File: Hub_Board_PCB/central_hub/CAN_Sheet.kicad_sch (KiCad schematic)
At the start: 18 parts, among them J1 CAN_OUT, U3 MCP2515-xST, U4 TJA1050, Y2 8M

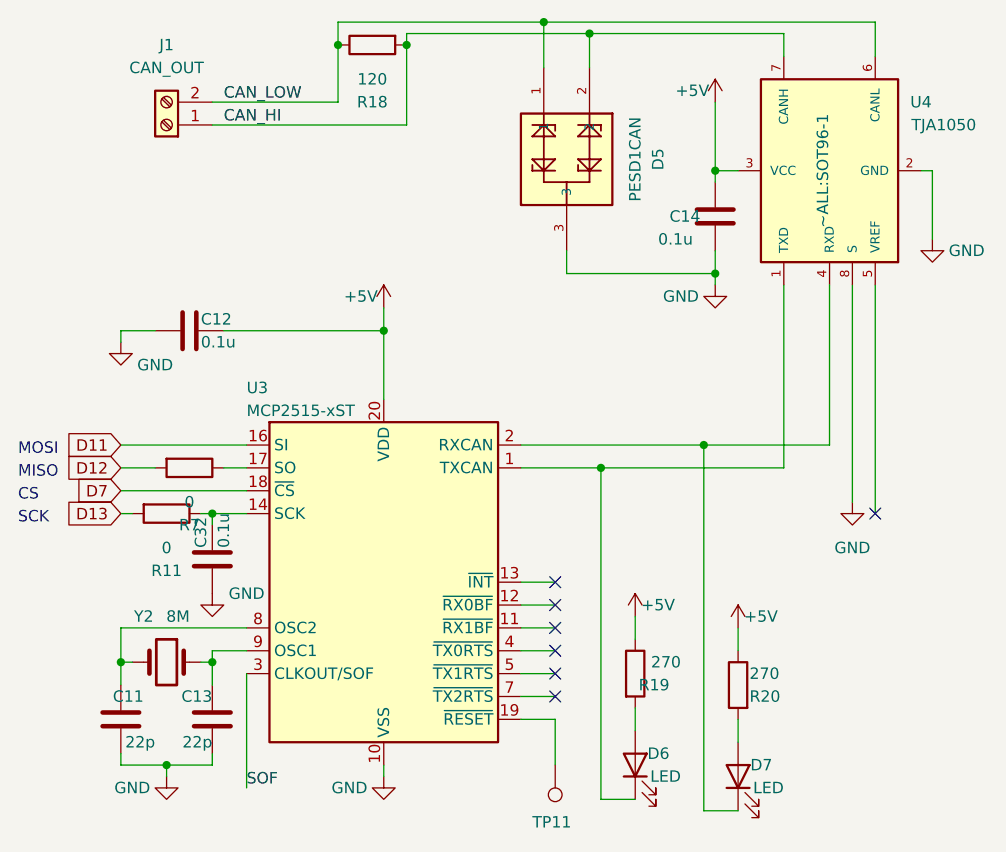
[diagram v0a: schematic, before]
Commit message: - added footprint labels to schematic
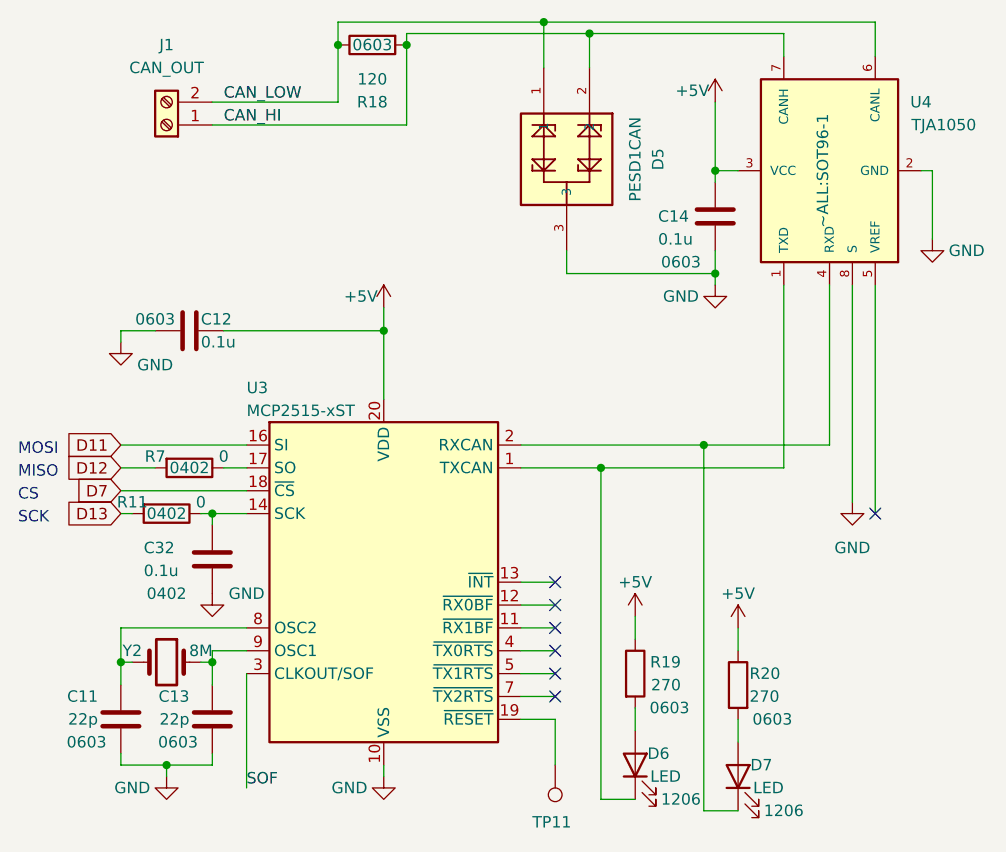
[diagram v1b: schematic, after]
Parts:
- C11, C12, C13, C14, R18, R19, R20: FP (none) -> 0603
- C32, R11, R7: FP (none) -> 0402
- D6, D7: FP (none) -> 1206
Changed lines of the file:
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@@
       (effects (font (size 1.27 1.27)) hide)
+    )
+    (property "FP" "1206" (at 101.6 107.95 90)
+      (effects (font (size 1.27 1.27)))
     )
     (pin "1")
@@
   (symbol (lib_id "Device:C") (at 38.1 97.79 180) (unit 1)
     (in_bom yes) (on_board yes) (dnp no)
-    (property "Reference" "C13" (at 38.1 95.25 0)
-      (effects (font (size 1.27 1.27)) (justify left))
-    )
-    (property "Value" "22p" (at 38.1 100.33 0)
+    (property "Reference" "C13" (at 35.56 95.25 0)
+      (effects (font (size 1.27 1.27)) (justify left))
+    )
+    (property "Value" "22p" (at 35.56 97.79 0)
       (effects (font (size 1.27 1.27)) (justify left))
     )
@@
       (effects (font (size 1.27 1.27)) hide)
     )
+    (property "FP" "0603" (at 34.29 100.33 0)
+      (effects (font (size 1.27 1.27)))
+    )
     (pin "1")
     (pin "2")
@@
       (effects (font (size 1.27 1.27)) hide)
     )
+    (property "FP" "0603" (at 31.75 53.34 90)
+      (effects (font (size 1.27 1.27)))
+    )
     (pin "1")
     (pin "2")
@@
   (symbol (lib_id "Device:C") (at 93.98 41.91 0) (unit 1)
     (in_bom yes) (on_board yes) (dnp no)
-    (property "Reference" "C14" (at 88.9 41.91 0)
+    (property "Reference" "C14" (at 87.63 41.91 0)
       (effects (font (size 1.27 1.27)) (justify left))
     )
@@
       (effects (font (size 1.27 1.27)) hide)
     )
+    (property "FP" "0603" (at 90.17 46.99 0)
+      (effects (font (size 1.27 1.27)))
+    )
     (pin "1")
     (pin "2")
@@
   (symbol (lib_id "Device:C") (at 27.94 97.79 180) (unit 1)
     (in_bom yes) (on_board yes) (dnp no)
-    (property "Reference" "C11" (at 30.48 95.25 0)
-      (effects (font (size 1.27 1.27)) (justify left))
-    )
-    (property "Value" "22p" (at 31.75 100.33 0)
+    (property "Reference" "C11" (at 25.4 95.25 0)
+      (effects (font (size 1.27 1.27)) (justify left))
+    )
+    (property "Value" "22p" (at 25.4 97.79 0)
       (effects (font (size 1.27 1.27)) (justify left))
     )
@@
       (effects (font (size 1.27 1.27)) hide)
     )
+    (property "FP" "0603" (at 24.13 100.33 0)
+      (effects (font (size 1.27 1.27)))
+    )
     (pin "1")
     (pin "2")
@@
   (symbol (lib_id "Device:R") (at 33.02 74.93 270) (unit 1)
     (in_bom yes) (on_board yes) (dnp no)
-    (property "Reference" "R11" (at 33.02 81.28 90)
-      (effects (font (size 1.27 1.27)))
-    )
-    (property "Value" "0" (at 33.02 78.74 90)
+    (property "Reference" "R11" (at 29.21 73.66 90)
+      (effects (font (size 1.27 1.27)))
+    )
+    (property "Value" "0" (at 36.83 73.66 90)
       (effects (font (size 1.27 1.27)))
     )
@@
       (effects (font (size 1.27 1.27)) hide)
     )
+    (property "FP" "0402" (at 33.02 74.93 90)
+      (effects (font (size 1.27 1.27)))
+    )
     (pin "1")
     (pin "2")
@@
       (effects (font (size 1.27 1.27)) hide)
     )
-    (property "Value" "+5V" (at 99.06 86.36 0)
+    (property "Value" "+5V" (at 96.52 83.82 0)
       (effects (font (size 1.27 1.27)))
     )
@@
   (symbol (lib_id "Device:C") (at 38.1 80.01 0) (unit 1)
     (in_bom yes) (on_board yes) (dnp no)
-    (property "Reference" "C32" (at 36.83 78.74 90)
-      (effects (font (size 1.27 1.27)) (justify left))
-    )
-    (property "Value" "0.1u" (at 39.37 78.74 90)
+    (property "Reference" "C32" (at 30.48 78.74 0)
+      (effects (font (size 1.27 1.27)) (justify left))
+    )
+    (property "Value" "0.1u" (at 30.48 81.28 0)
       (effects (font (size 1.27 1.27)) (justify left))
     )
@@
       (effects (font (size 1.27 1.27)) hide)
     )
+    (property "FP" "0402" (at 33.02 83.82 0)
+      (effects (font (size 1.27 1.27)))
+    )
     (pin "1")
     (pin "2")
@@
       (effects (font (size 1.27 1.27)) hide)
     )
-    (property "Value" "+5V" (at 87.63 85.09 0)
+    (property "Value" "+5V" (at 85.09 82.55 0)
       (effects (font (size 1.27 1.27)))
     )
@@
   (symbol (lib_id "Device:R") (at 96.52 93.98 0) (mirror y) (unit 1)
     (in_bom yes) (on_board yes) (dnp no)
-    (property "Reference" "R20" (at 97.79 95.25 0)
+    (property "Reference" "R20" (at 97.79 92.71 0)
       (effects (font (size 1.27 1.27)) (justify right))
     )
-    (property "Value" "270" (at 97.79 92.71 0)
+    (property "Value" "270" (at 97.79 95.25 0)
       (effects (font (size 1.27 1.27)) (justify right))
     )
@@
       (effects (font (size 1.27 1.27)) hide)
     )
+    (property "FP" "0603" (at 100.33 97.79 0)
+      (effects (font (size 1.27 1.27)))
+    )
     (pin "1")
     (pin "2")
@@
   (symbol (lib_id "Device:Crystal") (at 33.02 91.44 0) (mirror y) (unit 1)
     (in_bom yes) (on_board yes) (dnp no)
-    (property "Reference" "Y2" (at 30.48 86.36 0)
-      (effects (font (size 1.27 1.27)))
-    )
-    (property "Value" "8M" (at 34.29 86.36 0)
+    (property "Reference" "Y2" (at 29.21 90.17 0)
+      (effects (font (size 1.27 1.27)))
+    )
+    (property "Value" "8M" (at 36.83 90.17 0)
       (effects (font (size 1.27 1.27)))
     )
@@
       (effects (font (size 1.27 1.27)) hide)
     )
+    (property "FP" "1206" (at 90.17 106.68 90)
+      (effects (font (size 1.27 1.27)))
+    )
     (pin "1")
     (pin "2")
@@
   (symbol (lib_id "Device:R") (at 85.09 92.71 0) (unit 1)
     (in_bom yes) (on_board yes) (dnp no)
-    (property "Reference" "R19" (at 88.9 93.98 0)
+    (property "Reference" "R19" (at 90.17 91.44 0)
       (effects (font (size 1.27 1.27)) (justify right))
     )
-    (property "Value" "270" (at 90.17 91.44 0)
+    (property "Value" "270" (at 90.17 93.98 0)
       (effects (font (size 1.27 1.27)) (justify right))
     )
@@
       (effects (font (size 1.27 1.27)) hide)
     )
+    (property "FP" "0603" (at 88.9 96.52 0)
+      (effects (font (size 1.27 1.27)))
+    )
     (pin "1")
     (pin "2")
@@
   (symbol (lib_id "Device:R") (at 35.56 69.85 270) (unit 1)
     (in_bom yes) (on_board yes) (dnp no)
-    (property "Reference" "R7" (at 35.56 76.2 90)
-      (effects (font (size 1.27 1.27)))
-    )
-    (property "Value" "0" (at 35.56 73.66 90)
+    (property "Reference" "R7" (at 31.75 68.58 90)
+      (effects (font (size 1.27 1.27)))
+    )
+    (property "Value" "0" (at 39.37 68.58 90)
       (effects (font (size 1.27 1.27)))
     )
@@
     (property "Datasheet" "~" (at 35.56 69.85 0)
       (effects (font (size 1.27 1.27)) hide)
+    )
+    (property "FP" "0402" (at 35.56 69.85 90)
+      (effects (font (size 1.27 1.27)))
     )
     (pin "1")
@@
       (effects (font (size 1.27 1.27)) hide)
     )
-    (pin "1")
+    (property "FP" "0603" (at 55.88 22.86 90)
+      (effects (font (size 1.27 1.27)))
+    )
+    (pin "1")
